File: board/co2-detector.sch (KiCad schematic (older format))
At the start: 10 parts, among them U1 WeMos_D1_mini, U2 SGP30

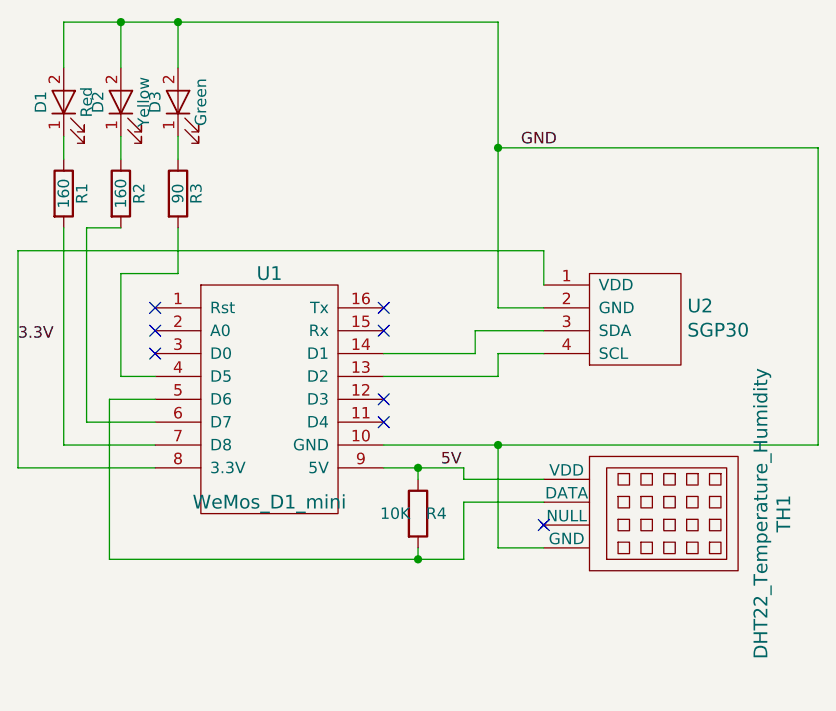
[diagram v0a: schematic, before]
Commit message: Board revision 2, fixes two desing problems
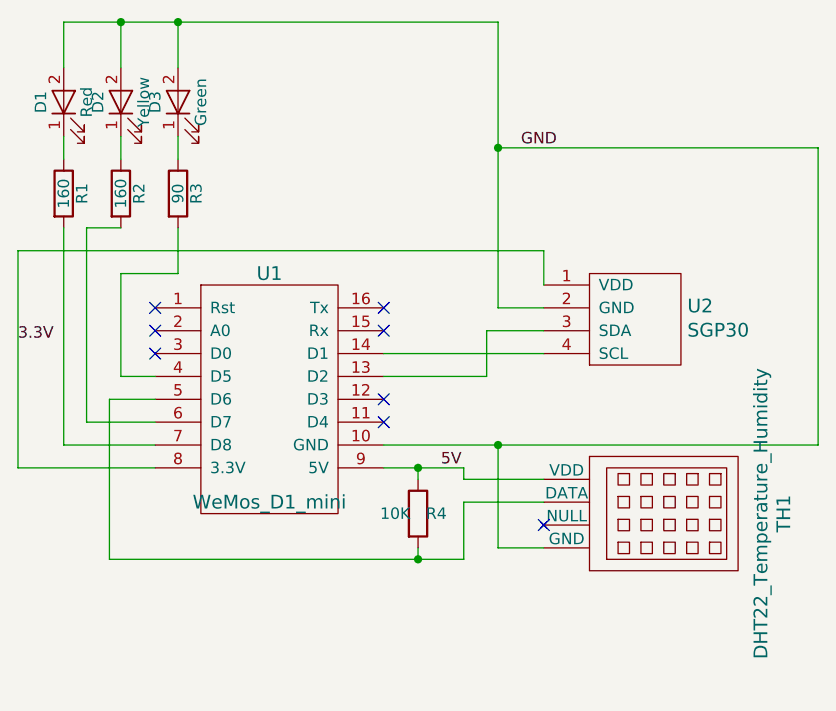
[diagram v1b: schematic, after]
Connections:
- net at U1.13 (D2): now also U2.3 (SDA); no longer U2.4 (SCL)
- net at U1.14 (D1): now also U2.4 (SCL); no longer U2.3 (SDA)
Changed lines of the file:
@@
 $EndComp
-Wire Wire Line
-	5300 2900 5300 2800
-Wire Wire Line
-	5300 2800 5600 2800
-Wire Wire Line
-	5600 2900 5400 2900
-Wire Wire Line
-	5400 2900 5400 3000
 Wire Wire Line
 	3300 2450 5600 2450
@@
 Wire Wire Line
 	4900 3300 5400 3300
-Wire Wire Line
-	5400 3000 4900 3000
-Wire Wire Line
-	4900 2900 5300 2900
 $Comp
 L co2-detector-rescue:WeMos_D1_mini-wemos_mini-meteo-home-rescue U1
@@
 Text Label 5150 3400 0    50   ~ 0
 5V
+Wire Wire Line
+	4900 2900 5600 2900
+Wire Wire Line
+	5600 2800 5350 2800
+Wire Wire Line
+	5350 2800 5350 3000
+Wire Wire Line
+	5350 3000 4900 3000
 $EndSCHEMATC
